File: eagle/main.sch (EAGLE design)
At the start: 31 parts, among them IC1 STM32F103RCT, IC2 LM1117IMPX-ADJ, Q1 8MHz

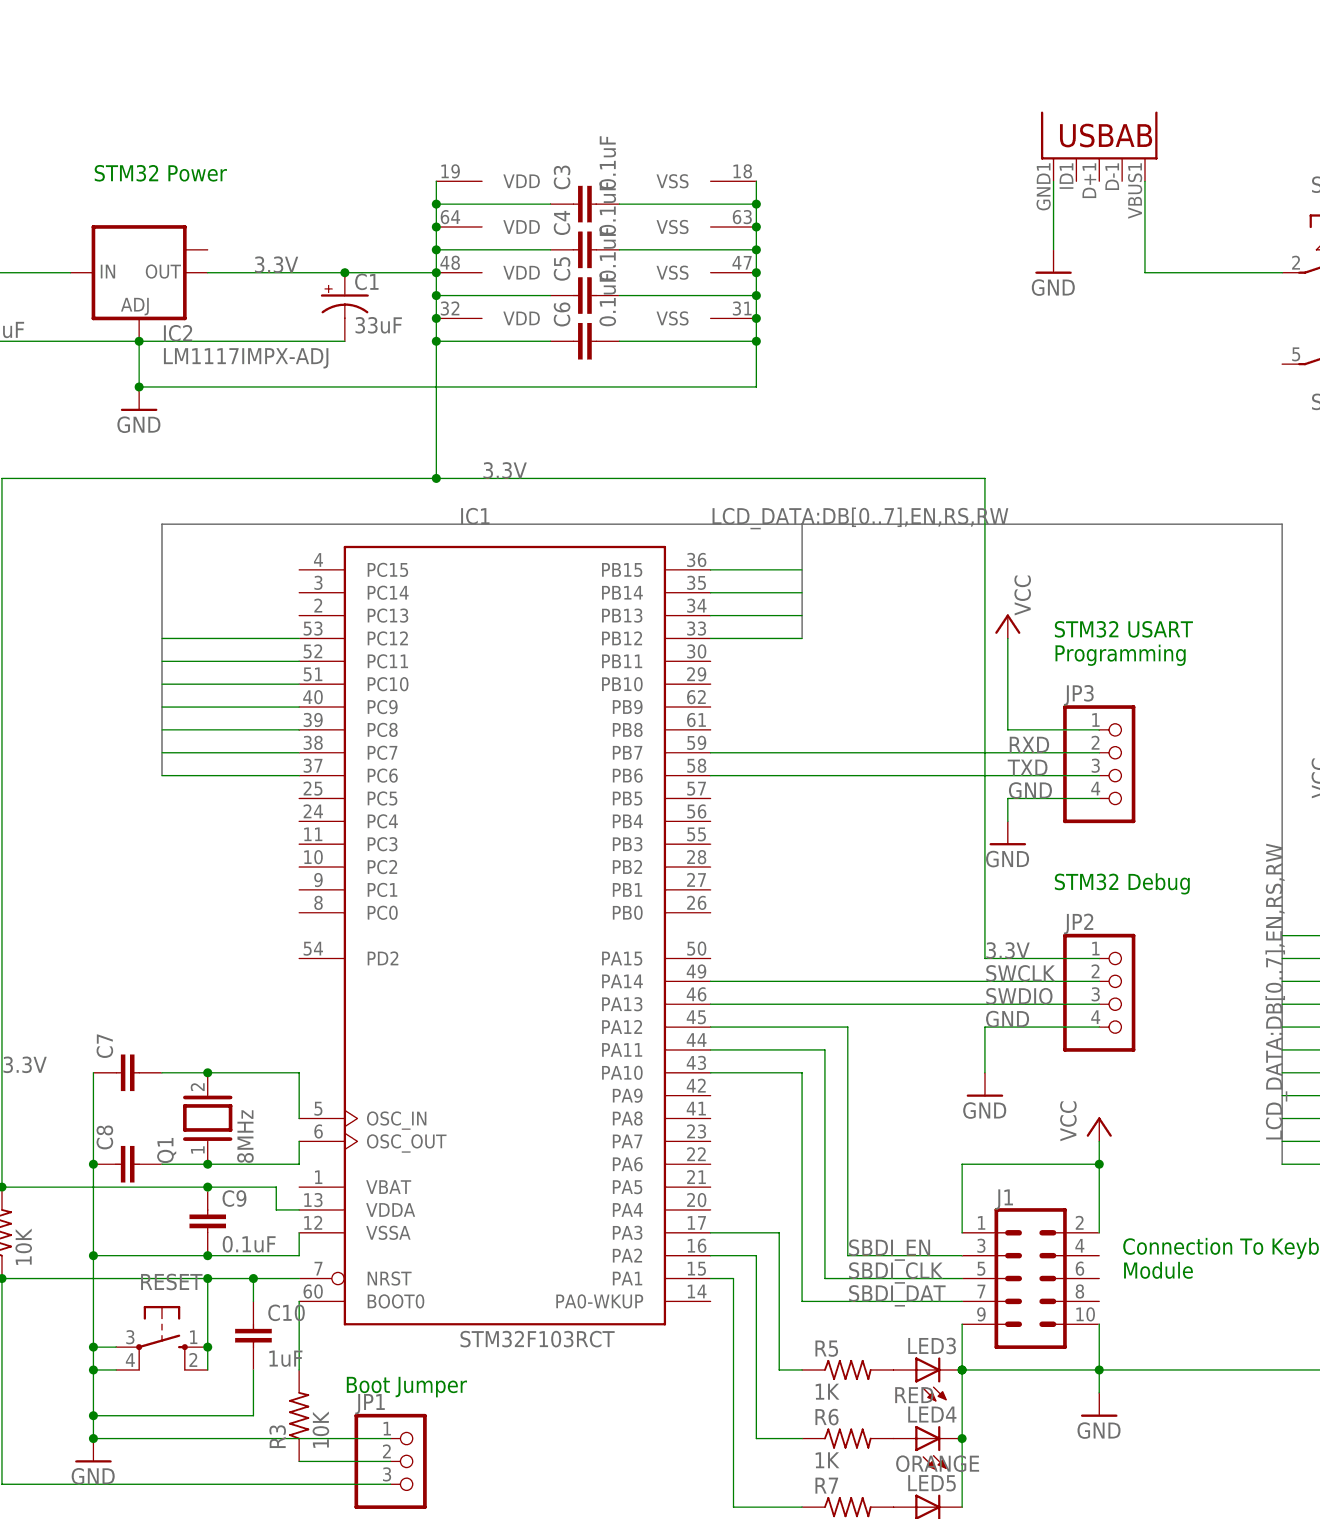
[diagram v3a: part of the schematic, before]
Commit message: Finish basic component placement
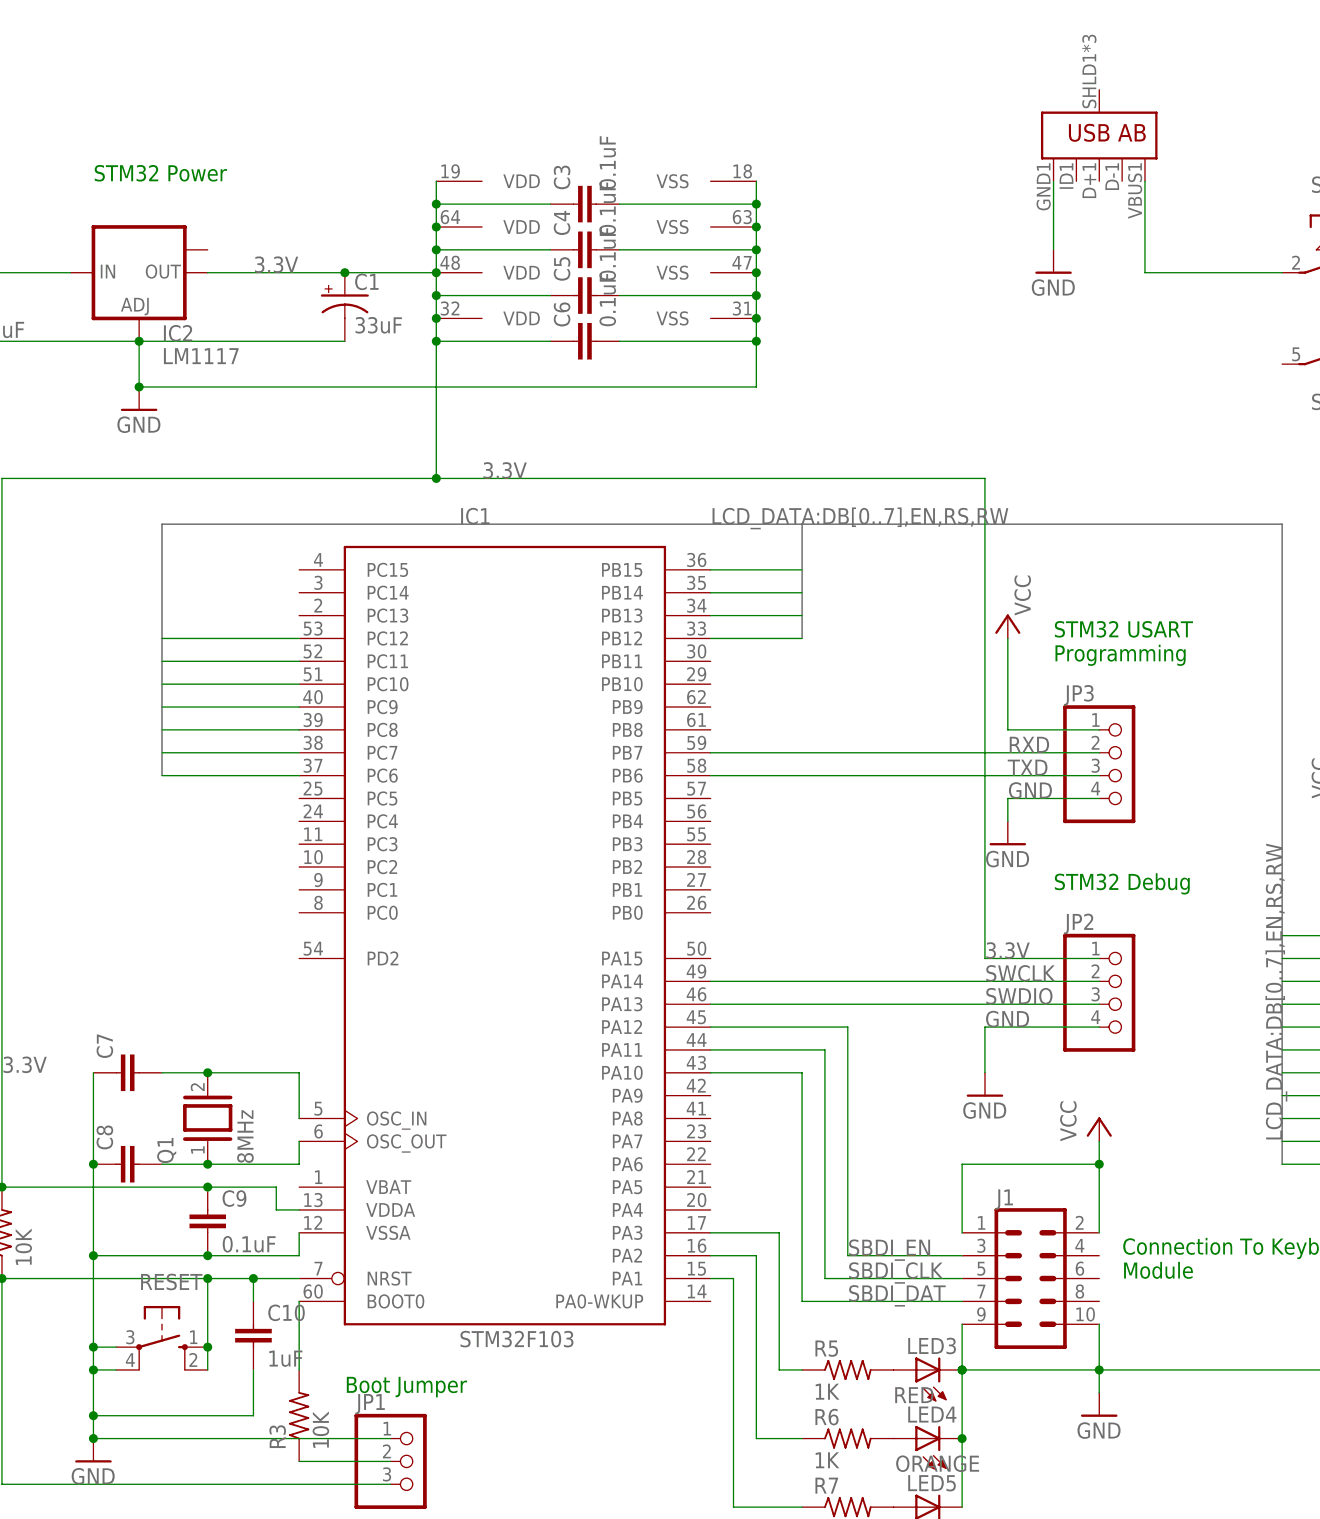
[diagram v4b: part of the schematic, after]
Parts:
- IC1: value STM32F103RCT -> STM32F103
- IC2: value LM1117IMPX-ADJ -> LM1117
- U1: device MicroUSB:USB"" -> SparkFun-Connectors:USB_AB_SMT
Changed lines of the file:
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@@
 <parts>
 <part name="FRAME1" library="frames" library_urn="urn:adsk.eagle:library:229" deviceset="A3L-LOC" device=""/>
-<part name="IC1" library="micro-stm_v3" deviceset="STM32F103R*T" device="" technology="C"/>
+<part name="IC1" library="micro-stm_v3" deviceset="STM32F103R*T" device="" technology="C" value="STM32F103"/>
 <part name="C1" library="rcl" library_urn="urn:adsk.eagle:library:334" deviceset="CPOL-US" device="E2-5" package3d_urn="urn:adsk.eagle:package:23346/2" value="33uF"/>
-<part name="IC2" library="lm1117" deviceset="LM1117IMPX-ADJ" device=""/>
+<part name="IC2" library="lm1117" deviceset="LM1117IMPX-ADJ" device="" value="LM1117"/>
 <part name="P+5" library="supply1" library_urn="urn:adsk.eagle:library:371" deviceset="VCC" device=""/>
 <part name="C2" library="rcl" library_urn="urn:adsk.eagle:library:334" deviceset="C-EU" device="025-025X050" package3d_urn="urn:adsk.eagle:package:23629/2" value="0.1uF"/>
@@
 <part name="LED5" library="led" library_urn="urn:adsk.eagle:library:259" deviceset="LED" device="5MM" package3d_urn="urn:adsk.eagle:package:15799/2" value="GREEN"/>
 <part name="S1" library="switch-misc" library_urn="urn:adsk.eagle:library:376" deviceset="PVA2R" device="" package3d_urn="urn:adsk.eagle:package:27428/1"/>
-<part name="U1" library="MicroUSB" deviceset="USB" device="&quot;&quot;"/>
+<part name="U1" library="SparkFun-Connectors" library_urn="urn:adsk.eagle:library:513" deviceset="USB_AB" device="_SMT" package3d_urn="urn:adsk.eagle:package:38266/1"/>
 <part name="GND1" library="supply1" library_urn="urn:adsk.eagle:library:371" deviceset="GND" device=""/>
 <part name="P+1" library="supply1" library_urn="urn:adsk.eagle:library:371" deviceset="VCC" device=""/>

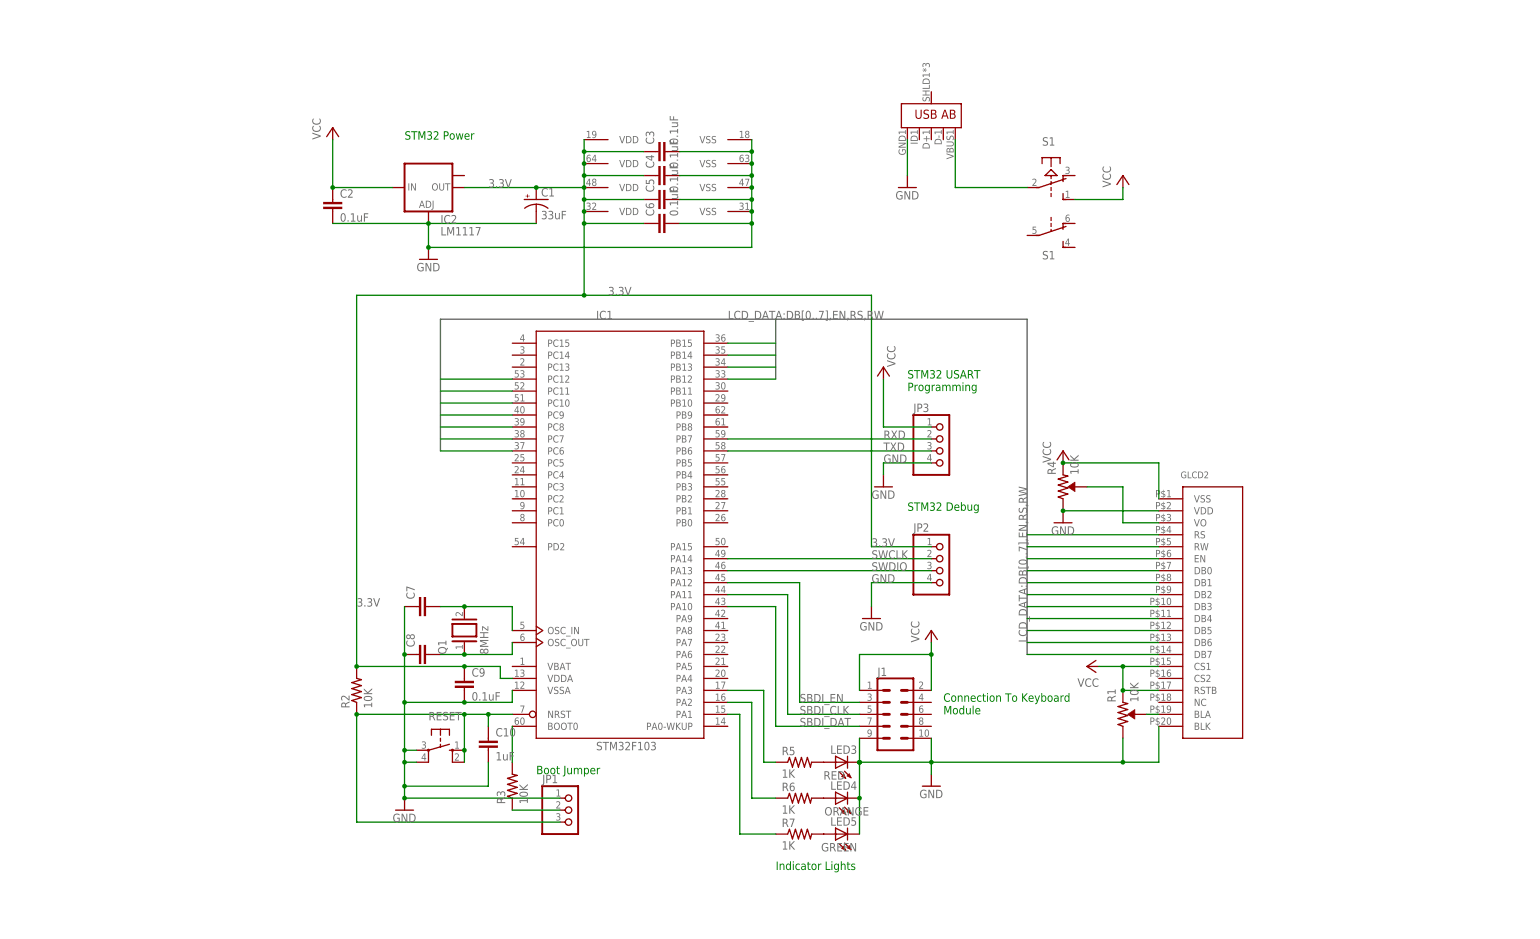
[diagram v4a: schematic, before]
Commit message: Route some nets in the main board
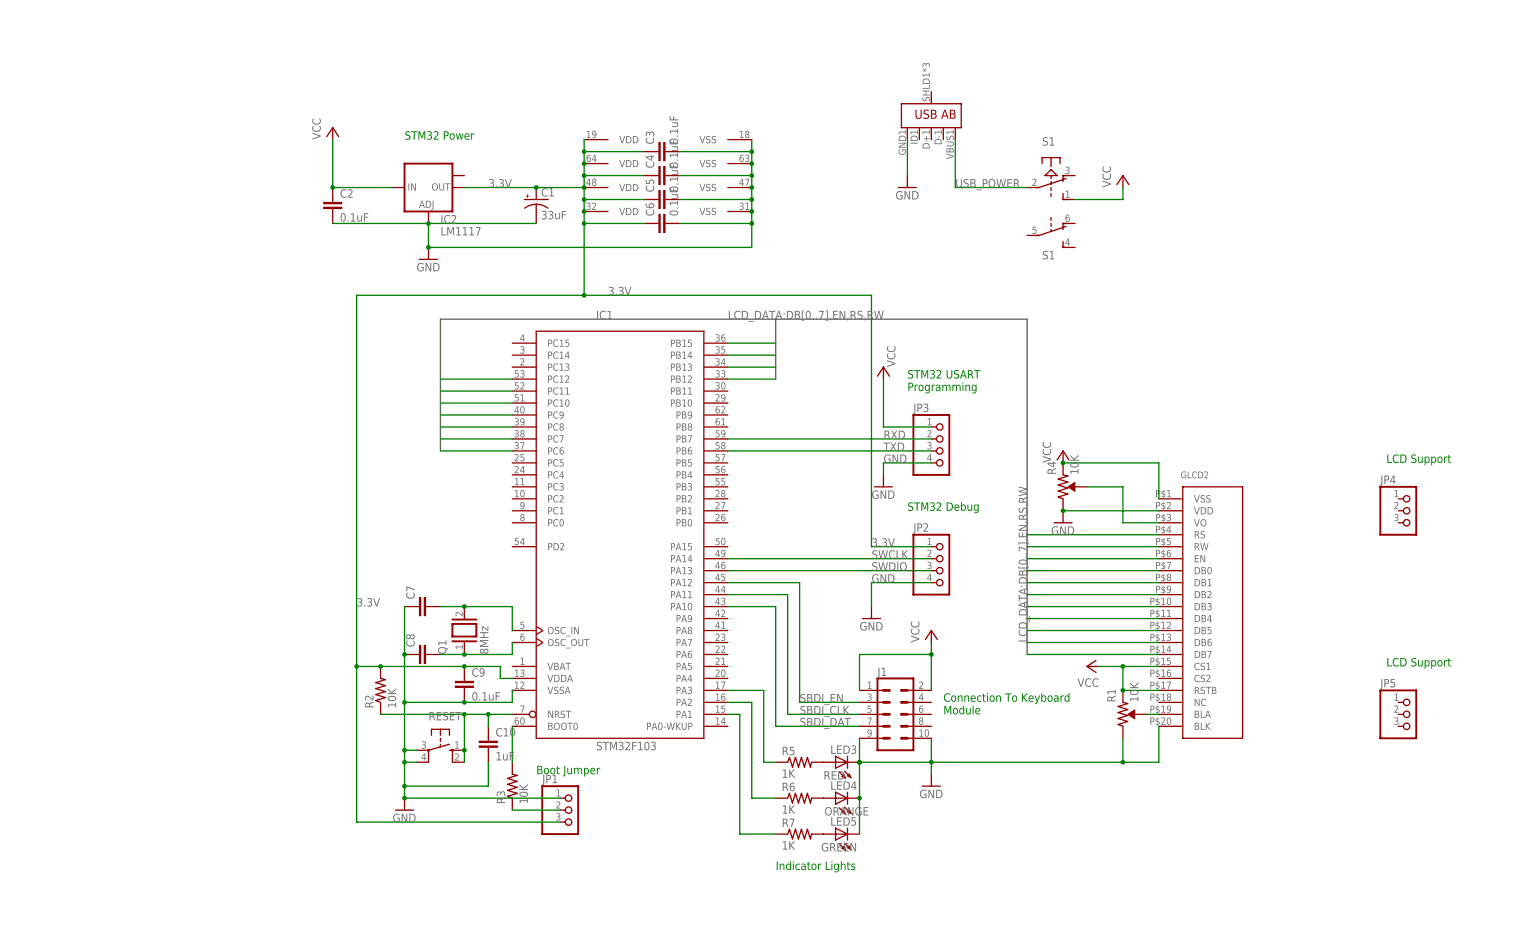
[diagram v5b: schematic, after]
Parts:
- added JP4, JP5: (no value), pinhead:PINHD-1X3
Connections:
- net N$8 renamed USB_POWER
- net 3.3V: now also JP1.3
- net N$6: no longer JP1.3
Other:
- note added: "LCD Support"
- moved on the sheet: R2
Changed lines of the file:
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@@
 <part name="GND1" library="supply1" library_urn="urn:adsk.eagle:library:371" deviceset="GND" device=""/>
 <part name="P+1" library="supply1" library_urn="urn:adsk.eagle:library:371" deviceset="VCC" device=""/>
+<part name="JP4" library="pinhead" library_urn="urn:adsk.eagle:library:325" deviceset="PINHD-1X3" device="" package3d_urn="urn:adsk.eagle:package:22458/2"/>
+<part name="JP5" library="pinhead" library_urn="urn:adsk.eagle:library:325" deviceset="PINHD-1X3" device="" package3d_urn="urn:adsk.eagle:package:22458/2"/>
 </parts>
 <sheets>
@@
 Module</text>
 <text x="-5.08" y="-73.66" size="1.778" layer="91">Indicator Lights</text>
+<text x="124.46" y="12.7" size="1.778" layer="91">LCD Support</text>
+<text x="124.46" y="-30.48" size="1.778" layer="91">LCD Support</text>
 </plain>
 <instances>
@@
 <attribute name="VALUE" x="-73.025" y="-44.45" size="1.778" layer="96"/>
 </instance>
-<instance part="R2" gate="G$1" x="-93.98" y="-35.56" smashed="yes" rot="R90">
-<attribute name="NAME" x="-95.4786" y="-39.37" size="1.778" layer="95" rot="R90"/>
-<attribute name="VALUE" x="-90.678" y="-39.37" size="1.778" layer="96" rot="R90"/>
+<instance part="R2" gate="G$1" x="-88.9" y="-35.56" smashed="yes" rot="R90">
+<attribute name="NAME" x="-90.3986" y="-39.37" size="1.778" layer="95" rot="R90"/>
+<attribute name="VALUE" x="-85.598" y="-39.37" size="1.778" layer="96" rot="R90"/>
 </instance>
 <instance part="C10" gate="G$1" x="-66.04" y="-45.72" smashed="yes">
@@
 <instance part="P+1" gate="VCC" x="68.58" y="73.66" smashed="yes">
 <attribute name="VALUE" x="66.04" y="71.12" size="1.778" layer="96" rot="R90"/>
+</instance>
+<instance part="JP4" gate="A" x="129.54" y="2.54" smashed="yes">
+<attribute name="NAME" x="123.19" y="8.255" size="1.778" layer="95"/>
+<attribute name="VALUE" x="123.19" y="-5.08" size="1.778" layer="96"/>
+</instance>
+<instance part="JP5" gate="A" x="129.54" y="-40.64" smashed="yes">
+<attribute name="NAME" x="123.19" y="-34.925" size="1.778" layer="95"/>
+<attribute name="VALUE" x="123.19" y="-48.26" size="1.778" layer="96"/>
 </instance>
 </instances>
@@
 <junction x="-45.72" y="63.5"/>
 <label x="-66.04" y="71.12" size="1.778" layer="95"/>
-<pinref part="R2" gate="G$1" pin="2"/>
-<pinref part="C9" gate="G$1" pin="1"/>
-<wire x1="-71.12" y1="-30.48" x2="-93.98" y2="-30.48" width="0.1524" layer="91"/>
-<junction x="-71.12" y="-30.48"/>
-<pinref part="IC1" gate="MCU" pin="VDDA"/>
-<wire x1="-60.96" y1="-33.02" x2="-63.5" y2="-33.02" width="0.1524" layer="91"/>
-<wire x1="-63.5" y1="-33.02" x2="-63.5" y2="-30.48" width="0.1524" layer="91"/>
-<wire x1="-63.5" y1="-30.48" x2="-71.12" y2="-30.48" width="0.1524" layer="91"/>
-<wire x1="-93.98" y1="-30.48" x2="-93.98" y2="48.26" width="0.1524" layer="91"/>
 <wire x1="-93.98" y1="48.26" x2="-45.72" y2="48.26" width="0.1524" layer="91"/>
-<junction x="-93.98" y="-30.48"/>
 <wire x1="-45.72" y1="48.26" x2="-45.72" y2="63.5" width="0.1524" layer="91"/>
 <pinref part="JP2" gate="A" pin="1"/>
@@
 <junction x="-45.72" y="48.26"/>
 <label x="-40.64" y="48.26" size="1.778" layer="95"/>
+<pinref part="R2" gate="G$1" pin="2"/>
+<pinref part="C9" gate="G$1" pin="1"/>
+<wire x1="-71.12" y1="-30.48" x2="-88.9" y2="-30.48" width="0.1524" layer="91"/>
+<junction x="-71.12" y="-30.48"/>
+<pinref part="IC1" gate="MCU" pin="VDDA"/>
+<wire x1="-60.96" y1="-33.02" x2="-63.5" y2="-33.02" width="0.1524" layer="91"/>
+<wire x1="-63.5" y1="-33.02" x2="-63.5" y2="-30.48" width="0.1524" layer="91"/>
+<wire x1="-63.5" y1="-30.48" x2="-71.12" y2="-30.48" width="0.1524" layer="91"/>
 <label x="-93.98" y="-17.78" size="1.778" layer="95"/>
+<wire x1="-93.98" y1="48.26" x2="-93.98" y2="-30.48" width="0.1524" layer="91"/>
+<wire x1="-93.98" y1="-30.48" x2="-88.9" y2="-30.48" width="0.1524" layer="91"/>
+<junction x="-88.9" y="-30.48"/>
+<pinref part="JP1" gate="A" pin="3"/>
+<wire x1="-50.8" y1="-63.5" x2="-93.98" y2="-63.5" width="0.1524" layer="91"/>
+<wire x1="-93.98" y1="-63.5" x2="-93.98" y2="-30.48" width="0.1524" layer="91"/>
+<junction x="-93.98" y="-30.48"/>
 </segment>
 </net>
@@
 <pinref part="R2" gate="G$1" pin="1"/>
 <pinref part="IC1" gate="MCU" pin="NRST"/>
-<wire x1="-93.98" y1="-40.64" x2="-71.12" y2="-40.64" width="0.1524" layer="91"/>
+<wire x1="-88.9" y1="-40.64" x2="-71.12" y2="-40.64" width="0.1524" layer="91"/>
 <pinref part="RESET" gate="1" pin="S"/>
 <wire x1="-71.12" y1="-40.64" x2="-66.04" y2="-40.64" width="0.1524" layer="91"/>
@@
 <wire x1="-66.04" y1="-43.18" x2="-66.04" y2="-40.64" width="0.1524" layer="91"/>
 <junction x="-66.04" y="-40.64"/>
-<pinref part="JP1" gate="A" pin="3"/>
-<wire x1="-50.8" y1="-63.5" x2="-93.98" y2="-63.5" width="0.1524" layer="91"/>
-<wire x1="-93.98" y1="-63.5" x2="-93.98" y2="-40.64" width="0.1524" layer="91"/>
-<junction x="-93.98" y="-40.64"/>
 </segment>
 </net>
@@
 </segment>
 </net>
-<net name="N$8" class="0">
+<net name="USB_POWER" class="0">
 <segment>
 <pinref part="U1" gate="G$1" pin="VBUS"/>
@@
 <pinref part="S1" gate="1" pin="P"/>
 <wire x1="33.02" y1="71.12" x2="48.26" y2="71.12" width="0.1524" layer="91"/>
-</segment>
-</net>
+<label x="33.02" y="71.12" size="1.778" layer="95"/>
+</segment>
+</net>
